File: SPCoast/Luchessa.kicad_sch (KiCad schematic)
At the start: 50 parts, among them SW7783 783, SW7795 795, SW7799 799

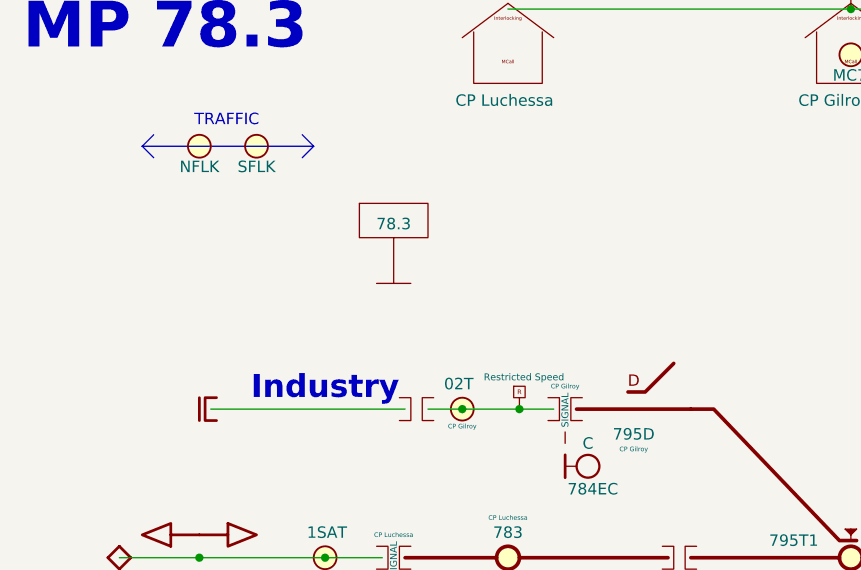
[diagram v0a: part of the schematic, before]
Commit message: chore(kicad): SPCoast symbols refreshed, field attribute visibility, no-connects on unused pins (owner's edit, baseline)
Owner, 2026-10-08: updated symbols from the libraries (the field pin direction flip, InterlockingPlant
61269e0), adjusted attribute visibility, added 22 no-connect markers on unused pins.

Verified (committed as saved, no edits):
- 485 components, 648 nets; every net identical to the previous commit.
- ERC 53 -> 20 messages (13 errors, 7 warnings). Remaining: unconnected HOUSE H / aux MC pins
  (Gilroy Caltrain, Luchessa, Watsonville); Corporal SW11901 still Railroad:Switch_HandThrow (not in
  the library) with open N/R legs; Sargent switch 1 open N/R legs; Christopher Panel U10029 A6 open
  while lamp LMP10093 carries a no-connect; 5 inherited wire stubs.
- Every instance path starts at the root uuid.

Co-Authored-By: Claude Opus 5.5 <noreply@anthropic.com>
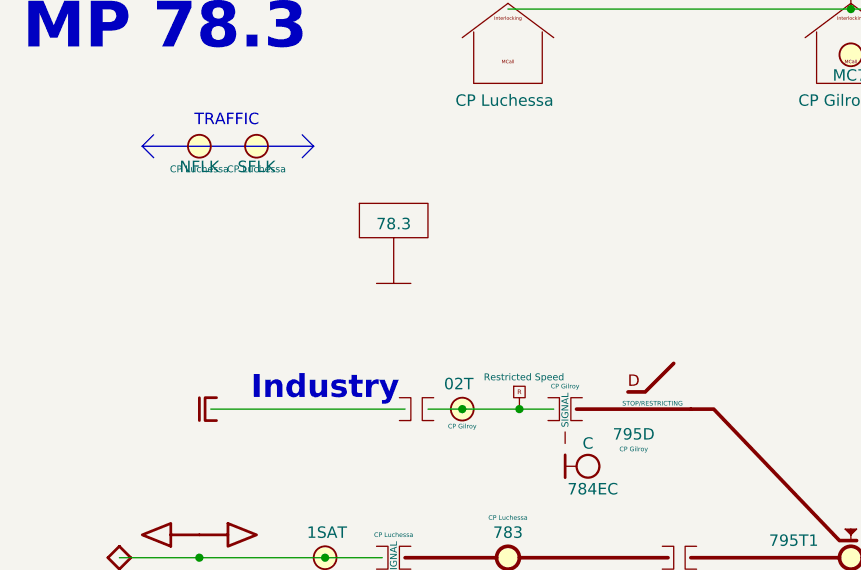
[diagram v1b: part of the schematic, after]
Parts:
- DERAIL7795: Indications (none) -> STOP/RESTRICTING
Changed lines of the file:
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@@
 		)
 		(property "CP" "CP Luchessa"
-			(at 43.18 40.64 0)
-			(hide yes)
+			(at 43.18 43.18 0)
 			(show_name no)
-			(do_not_autoplace no)
+			(do_not_autoplace yes)
 			(effects
 				(font
-					(size 1.27 1.27)
+					(size 0.762 0.762)
 				)
 			)
@@
 			(at 180.34 83.82 0)
 			(show_name no)
-			(do_not_autoplace no)
+			(do_not_autoplace yes)
 			(effects
 				(font
@@
 		)
 		(property "Role" "APPLIANCE"
-			(at 172.72 86.36 0)
+			(at 164.465 78.74 0)
 			(hide yes)
 			(show_name no)
@@
 		)
 		(property "Kind" "SWITCH_REMOTE"
-			(at 172.72 86.36 0)
+			(at 167.005 80.645 0)
 			(hide yes)
 			(show_name no)
@@
 			)
 		)
+		(property "Indications" ""
+			(at 186.055 85.725 0)
+			(show_name no)
+			(do_not_autoplace no)
+			(effects
+				(font
+					(size 0.508 0.508)
+				)
+			)
+		)
 		(pin "2"
 		)
@@
 		)
 		(property "Role" "APPLIANCE"
-			(at 109.22 86.36 0)
+			(at 116.205 80.01 0)
 			(hide yes)
 			(show_name no)
@@
 		)
 		(property "Kind" "SWITCH_LOCK"
-			(at 109.22 86.36 0)
+			(at 114.935 81.915 0)
 			(hide yes)
 			(show_name no)
@@
 			)
 		)
+		(property "Indications" ""
+			(at 95.885 85.725 0)
+			(show_name no)
+			(do_not_autoplace no)
+			(effects
+				(font
+					(size 0.508 0.508)
+				)
+			)
+		)
 		(pin "3"
 		)
@@
 		)
 		(property "CP" "CP Luchessa"
-			(at 36.83 40.64 0)
-			(hide yes)
+			(at 36.83 43.18 0)
 			(show_name no)
-			(do_not_autoplace no)
+			(do_not_autoplace yes)
 			(effects
 				(font
-					(size 1.27 1.27)
+					(size 0.762 0.762)
 				)
 			)
@@
 			(at 78.74 88.9 0)
 			(show_name no)
-			(do_not_autoplace no)
+			(do_not_autoplace yes)
 			(effects
 				(font
@@
 		)
 		(property "Role" "APPLIANCE"
-			(at 71.12 86.36 0)
+			(at 62.865 93.98 0)
 			(hide yes)
 			(show_name no)
@@
 		)
 		(property "Kind" "SWITCH_REMOTE"
-			(at 71.12 86.36 0)
+			(at 65.405 92.075 0)
 			(hide yes)
 			(show_name no)
@@
 			)
 		)
+		(property "Indications" ""
+			(at 84.455 86.995 0)
+			(show_name no)
+			(do_not_autoplace no)
+			(effects
+				(font
+					(size 0.508 0.508)
+				)
+			)
+		)
 		(pin "2"
 		)
@@
 			)
 		)
+		(property "Indications" "STOP/RESTRICTING"
+			(at 83.82 69.215 0)
+			(show_name no)
+			(do_not_autoplace no)
+			(effects
+				(font
+					(size 0.508 0.508)
+				)
+				(justify left)
+			)
+		)

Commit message: fix(kicad): SPCoast ERC clean: Corporal SW11901 to Switch_Manual_Sensed, Christopher lamp fixed, no-connects (owner's edit, baseline)
Owner, 2026-10-08. Corporal and Sargent's industry tracks (the beet loader) join each other outside
CTC: dark track, no routes, no NextCP.

Verified (committed as saved, no edits): 485 components, 648 nets; ERC 0 errors, 0 warnings.

Co-Authored-By: Claude Opus 5.5 <noreply@anthropic.com>
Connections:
- no-connect marks 0 -> 4
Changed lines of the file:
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@@
 		(color 0 0 0 0)
+	)
+	(no_connect
+		(at 36.83 40.64)
+	)
+	(no_connect
+		(at 43.18 40.64)
+	)
+	(no_connect
+		(at 172.72 30.48)
+	)
+	(no_connect
+		(at 71.12 30.48)
 	)
 	(wire

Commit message: feat(spcoast): every sheet on the four Railroad libraries (checkpoint step 6, mechanical half)
By SPCoast/edits/2026-10-12-migrate-libraries.py, run once with KiCad closed: 483 instances
remapped across 16 sheets, embedded definitions replaced by the library blocks, instance fields
synced (Kind, ControlToken, Vital, NormalIs, Chain, Index dropped; Indications renamed
IndicationCeiling; Hold_ms renamed hold_ms; a pixel's Index became its Address; Rulebook kept
on the four Luchessa markers because the compiler still reads it), and 22 units added at the
same position for the plates and devices that are multi-unit now. Owner's choices: every plant
head CPL; Sargent's semaphore UQ; the 0x27 PCA9685 as PWM; the office MAX7313s as the
SPCoastcTc variant. Left by hand: the two AUXILIARY_TRAFFIC markers on Watsonville (retired).

Verified (production/migration-gate.txt, netlist_diff.py against pre-migration.net): office
and local plates and all chips keep their connectivity; 14 nets lost, all on Sargent, where
the six field devices (DevSW13001, 13004 to 13007, 13012) have new pin positions and must be
re-wired by hand. ERC: lib_symbol_issues 492 before (unregistered libraries) to 2 after (the
retired markers); the 29 unconnected pins are those devices and their chip pins.

Co-Authored-By: Claude Fable 5.1 <noreply@anthropic.com>
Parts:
- B7001, B7003, B7004, B7008, B7009: symbol Railroad:IRJ-Signal -> Railroad-Trackplan:IRJ-Signal
- B7002, B7005, B7006, B7010: symbol Railroad:IRJ -> Railroad-Trackplan:IRJ
- B7007: symbol Railroad:Bumper -> Railroad-Trackplan:Bumper
- CP7001, CP7002, CP7003, CP7004: symbol Railroad:NextCP -> Railroad-Trackplan:NextCP
- DERAIL7795: symbol Railroad:Switch_Powered_Derail -> Railroad-Trackplan:Derail; Appliance (none) -> switch; IndicationCeiling (none) -> STOP/RESTRICTING; Indications STOP/RESTRICTING -> (none); Kind DERAIL -> (none); Style (none) -> derail
- DOT7001: symbol Railroad:Rule251-DoT-Left -> Railroad-Trackplan:Rule251-DoT-Left
- DOT7002: symbol Railroad:Rule251-DoT-Right -> Railroad-Trackplan:Rule251-DoT-Right
- DOT7003, DOT7004: symbol Railroad:Rule261-DoT-BiDirectional -> Railroad-Trackplan:Rule261-DoT-BiDirectional
- DOT7006: symbol Railroad:Rule105-RestrictedSpeed -> Railroad-Trackplan:Rule105-RestrictedSpeed
- FLK7001, FLK7002: symbol Railroad:AUXILIARY -> Railroad-Trackplan:AUXILIARY; Appliance (none) -> lamp; Kind AUXILIARY -> (none); Style (none) -> non_vital
- H7001, H7002, H7003, H7004, H7006, H7007, H7008: symbol Railroad:Signal Head - CL -> Railroad-Trackplan:Signal Head - CPL; Appliance (none) -> head; Kind HEAD -> (none); Style (none) -> CPL
- HOUSE7001, HOUSE7002, HOUSE7003: symbol Railroad:MAIN HOUSE -> Railroad-Trackplan:MAIN HOUSE
- MC7001: symbol Railroad:MaintainerCall -> Railroad-Trackplan:MaintainerCall; Appliance (none) -> lamp; Kind MAINTAINER_CALL -> (none); Style (none) -> maintainer_call
- MP7001, MP7002: symbol Railroad:Milepost -> Railroad-Trackplan:Milepost; Kind (none) -> MILEPOST
- Plant7001: symbol Railroad:Interlocking -> Railroad-Trackplan:Interlocking
- S784E1, S784W2: symbol Railroad:Mast_Double -> Railroad-Trackplan:Mast_Double; Appliance (none) -> mast; Kind MAST_DOUBLE -> (none); Style (none) -> double
- S784E2: symbol Railroad:Mast_Dwarf -> Railroad-Trackplan:Mast_Dwarf; Appliance (none) -> mast; Kind MAST_DWARF -> (none); Style (none) -> dwarf
- S784W1, S784W3: symbol Railroad:Mast_Single -> Railroad-Trackplan:Mast_Single; Appliance (none) -> mast; Kind MAST_SINGLE -> (none); Style (none) -> single
- SW7783, SW7799: symbol Railroad:Switch_Powered -> Railroad-Trackplan:Switch_Powered; Appliance (none) -> switch; Kind SWITCH_REMOTE -> (none); Style (none) -> powered
- SW7795: symbol Railroad:Switch_Lock -> Railroad-Trackplan:Switch_Lock; Appliance (none) -> switch; Kind SWITCH_LOCK -> (none); Style (none) -> lock
- TC7001, TC7002, TC7003, TC7004, TC7005, TC7006: symbol Railroad:Track Circuit -> Railroad-Trackplan:Track Circuit; Appliance (none) -> track_circuit; Kind TRACK_CIRCUIT -> (none)

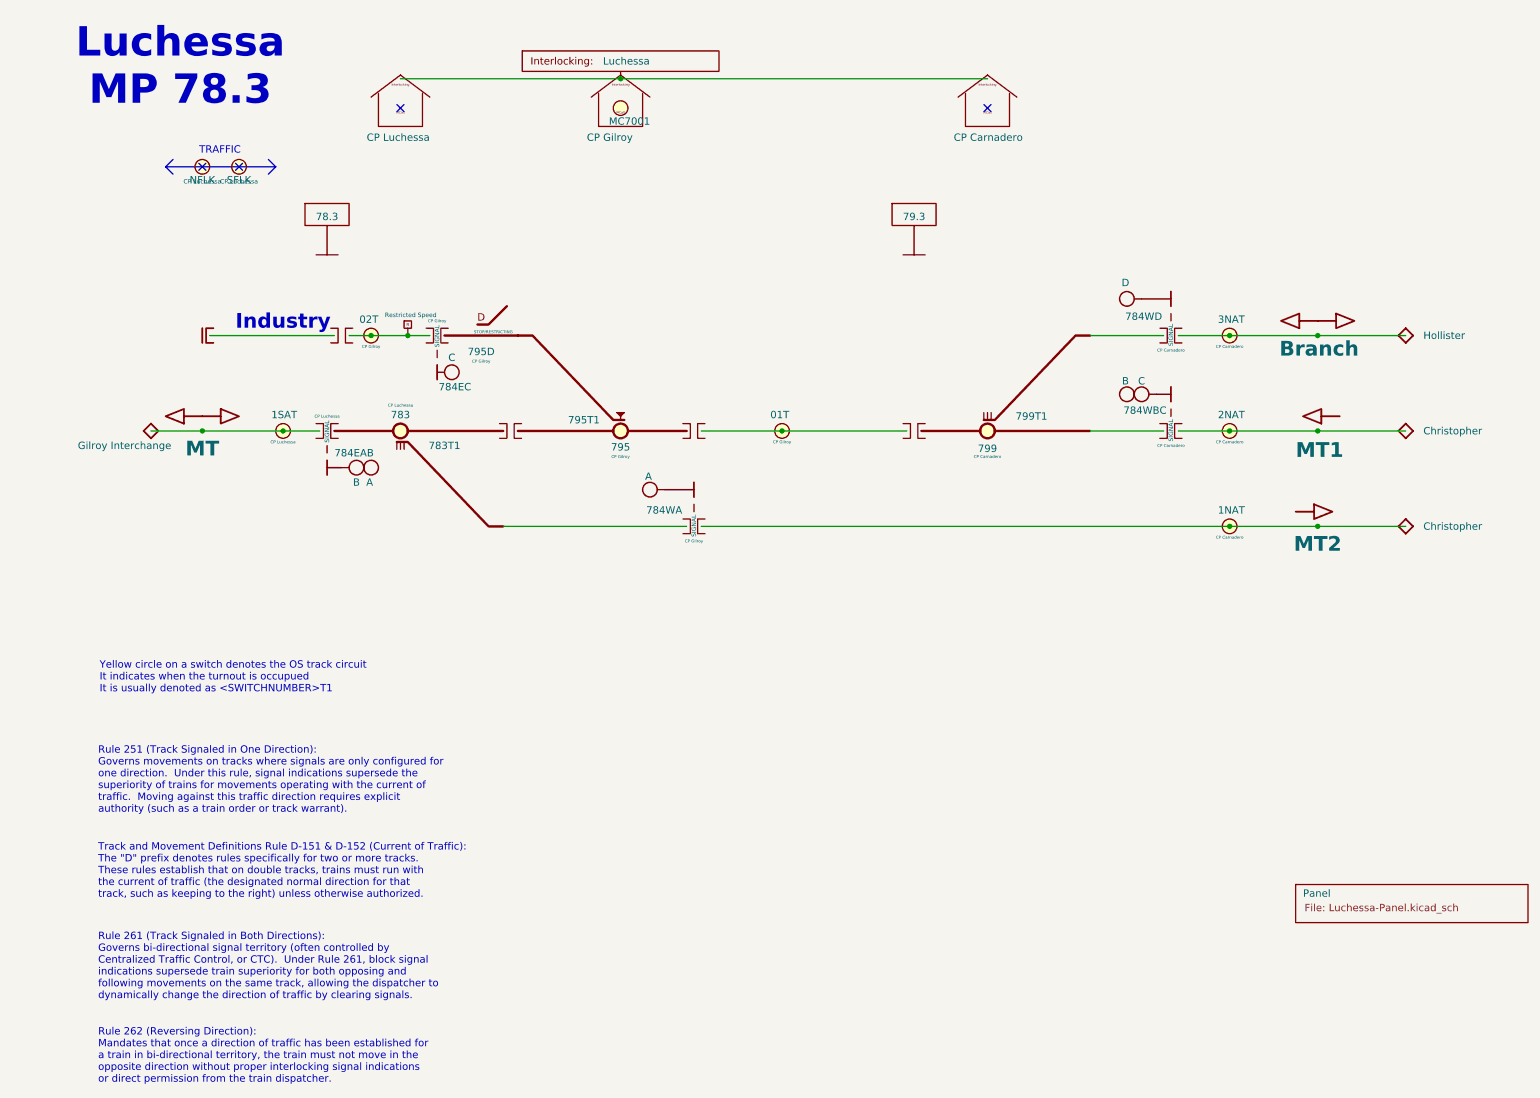
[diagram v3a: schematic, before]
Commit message: chore: owner's Sargent cleanup and library edits of 2026-10-12 and 13 (baseline)
Co-Authored-By: Claude Fable 5.1 <noreply@anthropic.com>
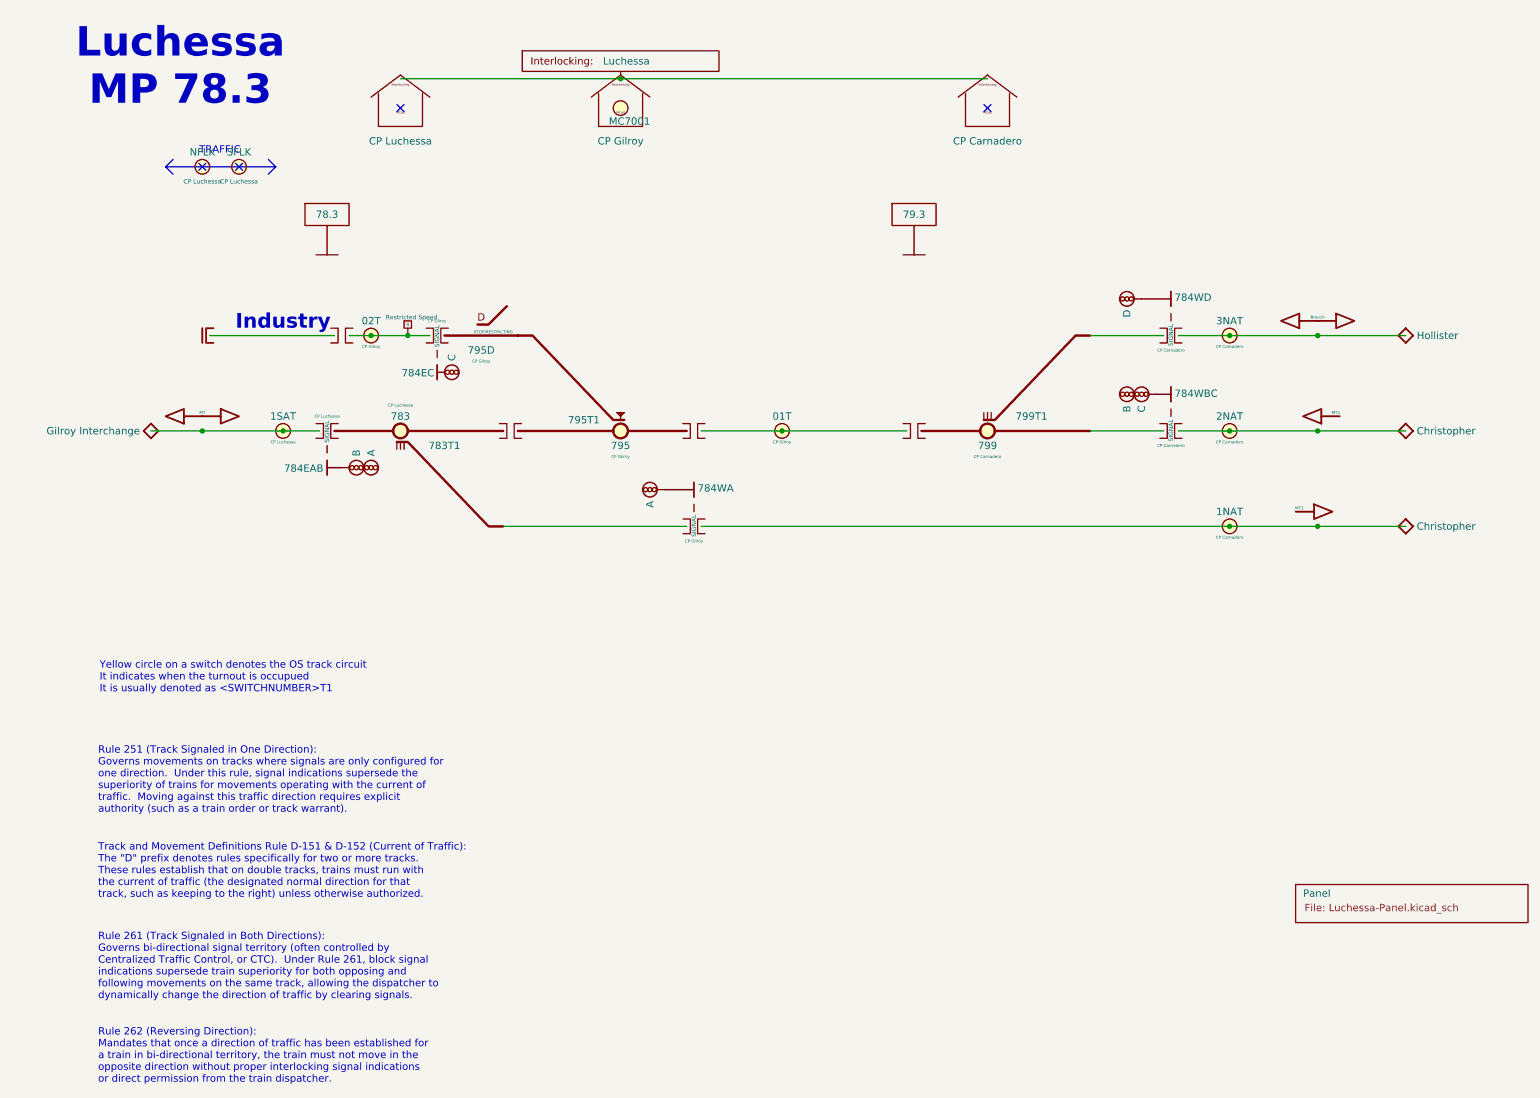
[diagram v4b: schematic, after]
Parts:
- DOT7001, DOT7002: Rulebook 251 -> (none)
- DOT7003, DOT7004: Rulebook 261 -> (none)

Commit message: fix(spcoast): placed instances agree with their library symbols on Role, Appliance, Style
KiCad copies fields at placement and never follows the library. The 2026-10-12 migration
filled empty instance fields but kept non-empty ones, so heads placed before the libraries
were corrected still said Role COMPONENT and Style CPL. A compiler joining devices to
appliances by Appliance and Style (I9) would have failed on Sargent's CL and UQ heads.

The one-off `SPCoast/edits/2026-10-16-sync-library-fields.py` sets every library-owned
field (Role, Appliance, Style, IC, Kind, Pin.*) on every instance of a Railroad-* symbol
to the library's value, by text edit. 58 instances on 7 sheets: 53 heads to Role APPLIANCE
(Sargent's H1 to Style UQ and H2 to CL), two Mileposts to Role TRACK (ADR 0004 D7), the
Sargent Local plates to Role DEVICE (checkpoint E72), and 836SB's semaphore device to the
library's Style list `LQ, UQ`.

Front-end rule this records (owner, 2026-10-16): library-owned fields are read from the
library by lib_id, and an instance that disagrees is a diagnostic.

Verified:
- tools/contract/netlist_diff.py production/SPCoast.net production/post-sync.net: 493 nets,
  1086 nodes, 485 parts, connectivity identical
- kicad-cli sch erc --severity-all: 0 violations
- the script re-run reports 0 changes

Co-Authored-By: Claude Fable 5.1 <noreply@anthropic.com>
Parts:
- H7001, H7002, H7003, H7004, H7006, H7007, H7008: Role COMPONENT -> APPLIANCE
- MP7001, MP7002: Role ANNOTATION -> TRACK
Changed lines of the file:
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@@
 			)
 		)
-		(property "Role" "COMPONENT"
+		(property "Role" "APPLIANCE"
 			(at 200.66 66.04 0)
 			(hide yes)
@@
 			)
 		)
-		(property "Role" "ANNOTATION"
+		(property "Role" "TRACK"
 			(at 58.42 55.88 0)
 			(hide yes)
@@
 			)
 		)
-		(property "Role" "COMPONENT"
+		(property "Role" "APPLIANCE"
 			(at 203.2 82.55 0)
 			(hide yes)
@@
 			)
 		)
-		(property "Role" "COMPONENT"
+		(property "Role" "APPLIANCE"
 			(at 62.23 90.17 0)
 			(hide yes)
@@
 			)
 		)
-		(property "Role" "COMPONENT"
+		(property "Role" "APPLIANCE"
 			(at 118.11 99.06 0)
 			(hide yes)
@@
 			)
 		)
-		(property "Role" "COMPONENT"
+		(property "Role" "APPLIANCE"
 			(at 59.69 90.17 0)
 			(hide yes)
@@
 			)
 		)
-		(property "Role" "COMPONENT"
+		(property "Role" "APPLIANCE"
 			(at 76.2 73.66 0)
 			(hide yes)
@@
 			)
 		)
-		(property "Role" "ANNOTATION"
+		(property "Role" "TRACK"
 			(at 160.02 55.88 0)
 			(hide yes)
@@
 			)
 		)
-		(property "Role" "COMPONENT"
+		(property "Role" "APPLIANCE"
 			(at 200.66 82.55 0)
 			(hide yes)

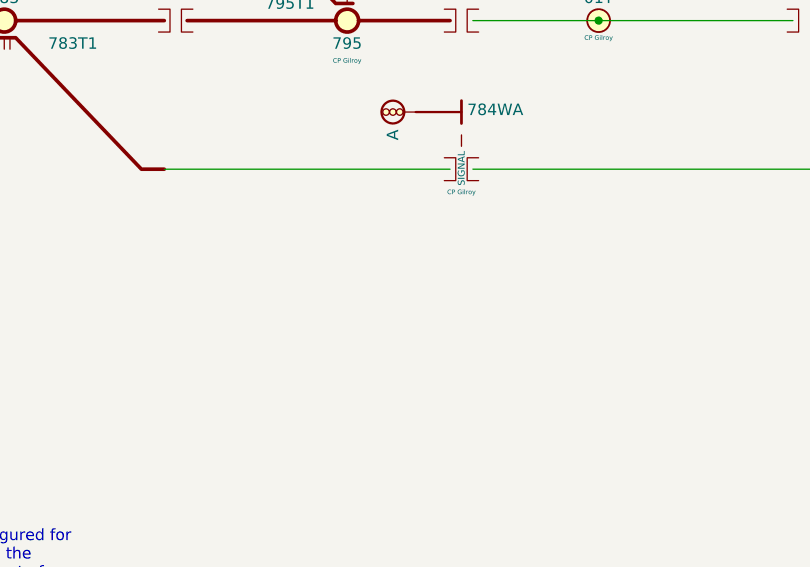
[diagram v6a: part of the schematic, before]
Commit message: chore(kicad): owner edits: GPIO drivers carry Address, Sargent I2C addresses, CMRI body text from fields
Baseline of the owner's saved work before the ADR 0005 scripts:
- Driver-GPIO-Digital and Driver-GPIO-Pixel gain an Address field (the
  board pin); Value renders ${Address}; body text and arrow adjusted.
- Driver-CMRI-IB/OB body text renders UA${Address}.IN/OUT.${Bit} from
  the fields instead of ${VALUE}.
- Sargent, Gilroy Interchange and Luchessa GPIO instances carry Address;
  Sargent Exp2 back at 0x26, Exp3 0x27.
- All sheets resaved by KiCad 10 (reordering), project file
  used_designators cleared by KiCad.

Verified: no lock files; committed as saved, unverified by netlist (the
baseline netlist is exported in the next step).

Co-Authored-By: Claude Fable 5.1 <noreply@anthropic.com>
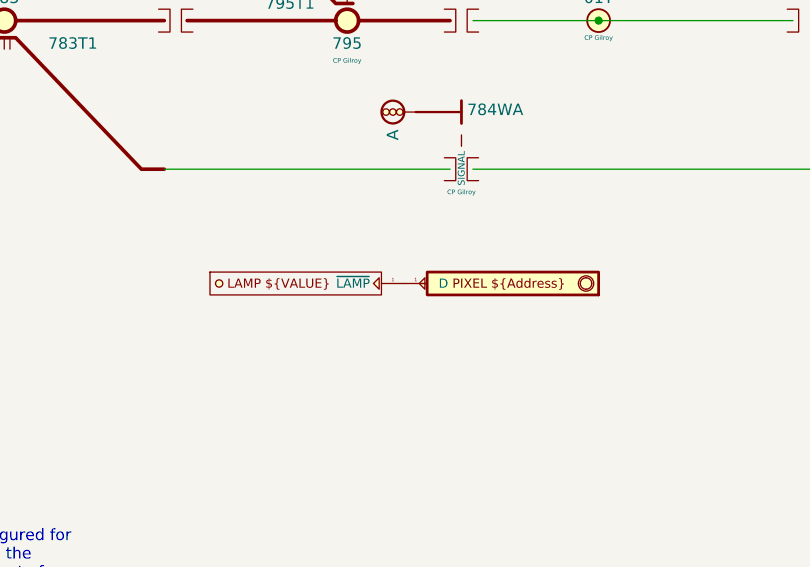
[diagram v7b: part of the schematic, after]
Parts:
- added DevLamp5: MC1K, symbol Railroad-Field:Device-Lamp
- added GPIO1: ${Address}, symbol Railroad-HardwareIO:Driver-GPIO-Pixel
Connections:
- new net: DevLamp5.1 (~{LAMP}), GPIO1.1 (D)
